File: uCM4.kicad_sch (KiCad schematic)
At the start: 71 parts, among them IC1 MAX17048G+, J10 USB_C_Receptacle, J12 Conn_02x08_Odd_Even, J13 Conn_02x07_Odd_Even, J2 Micro_SD_Card_Det, J4 Conn_01x04, J5 DummyJ, J6 DummyJ, J8 Camera 0, J9 Camera 1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

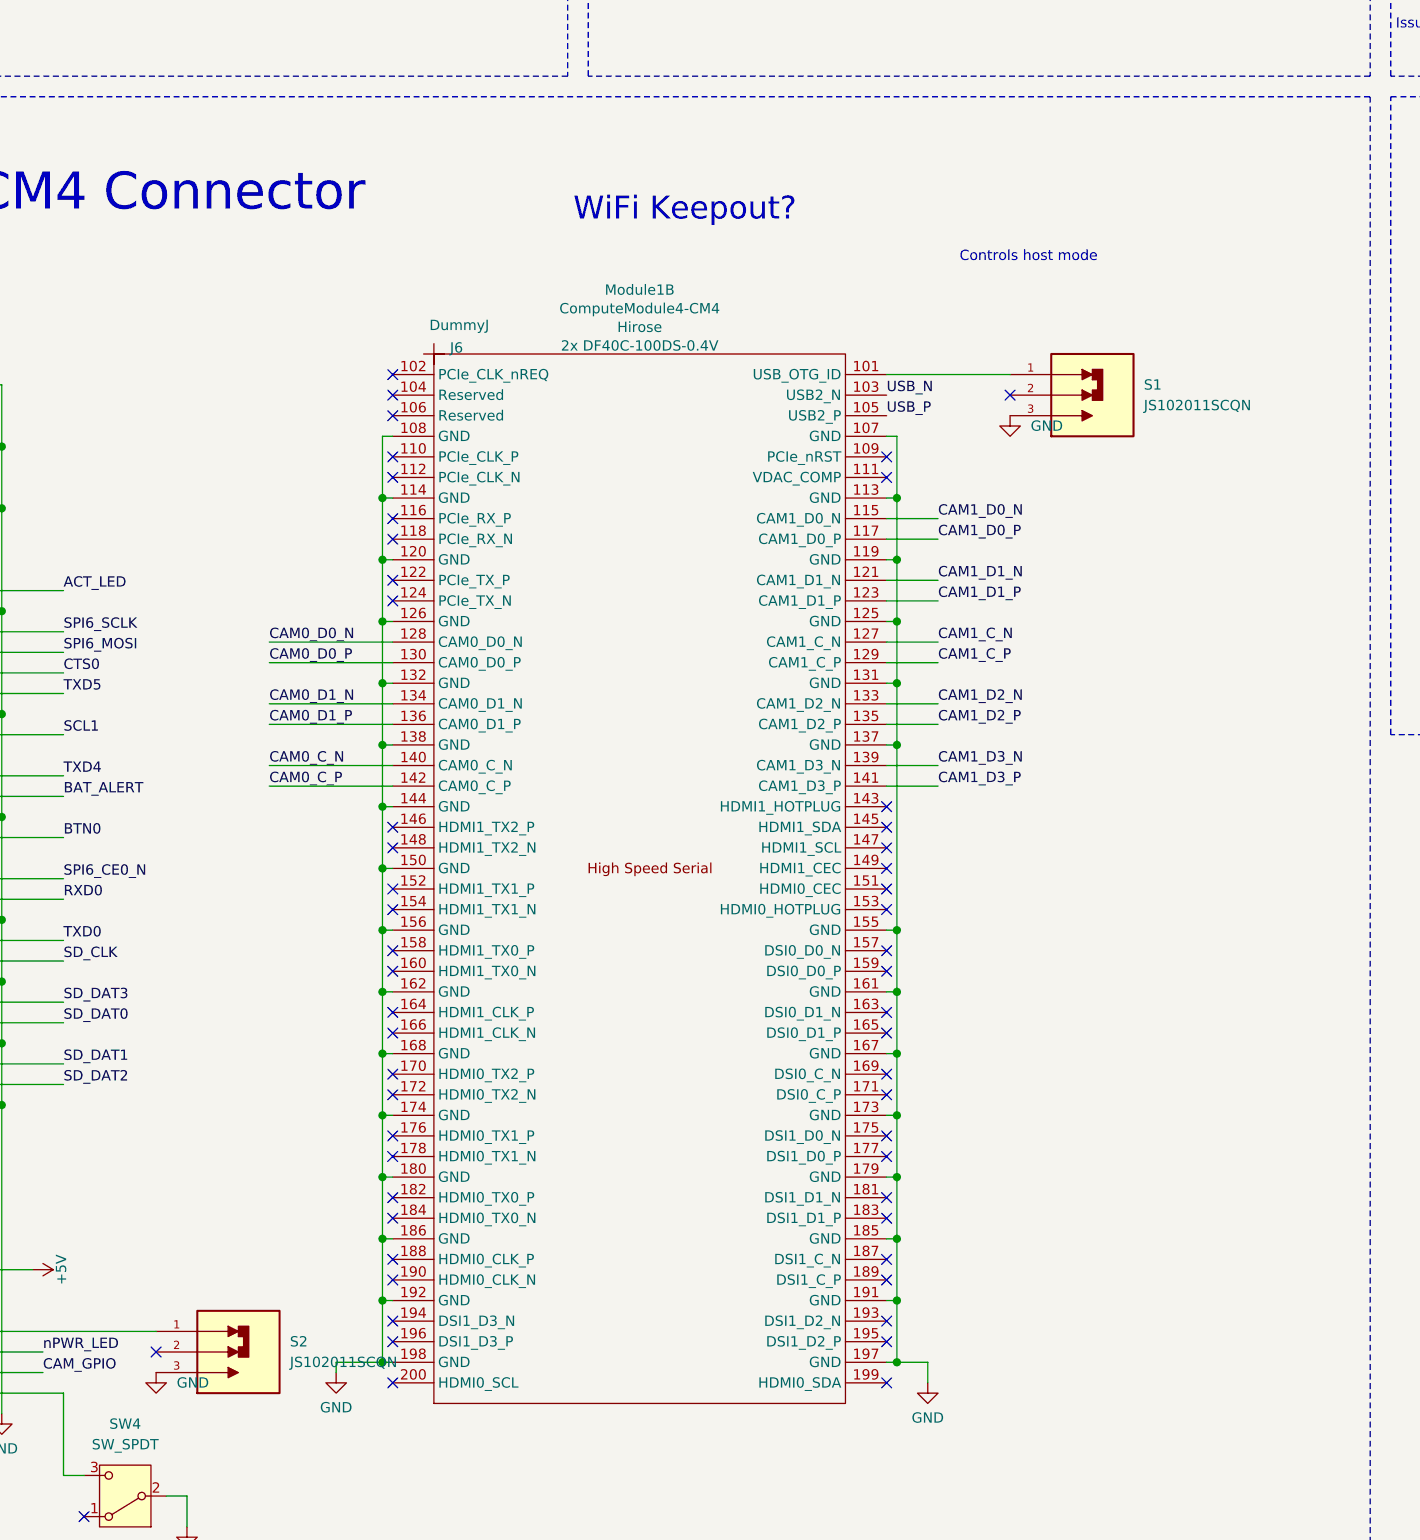
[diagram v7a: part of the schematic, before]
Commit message: Fixed switches.
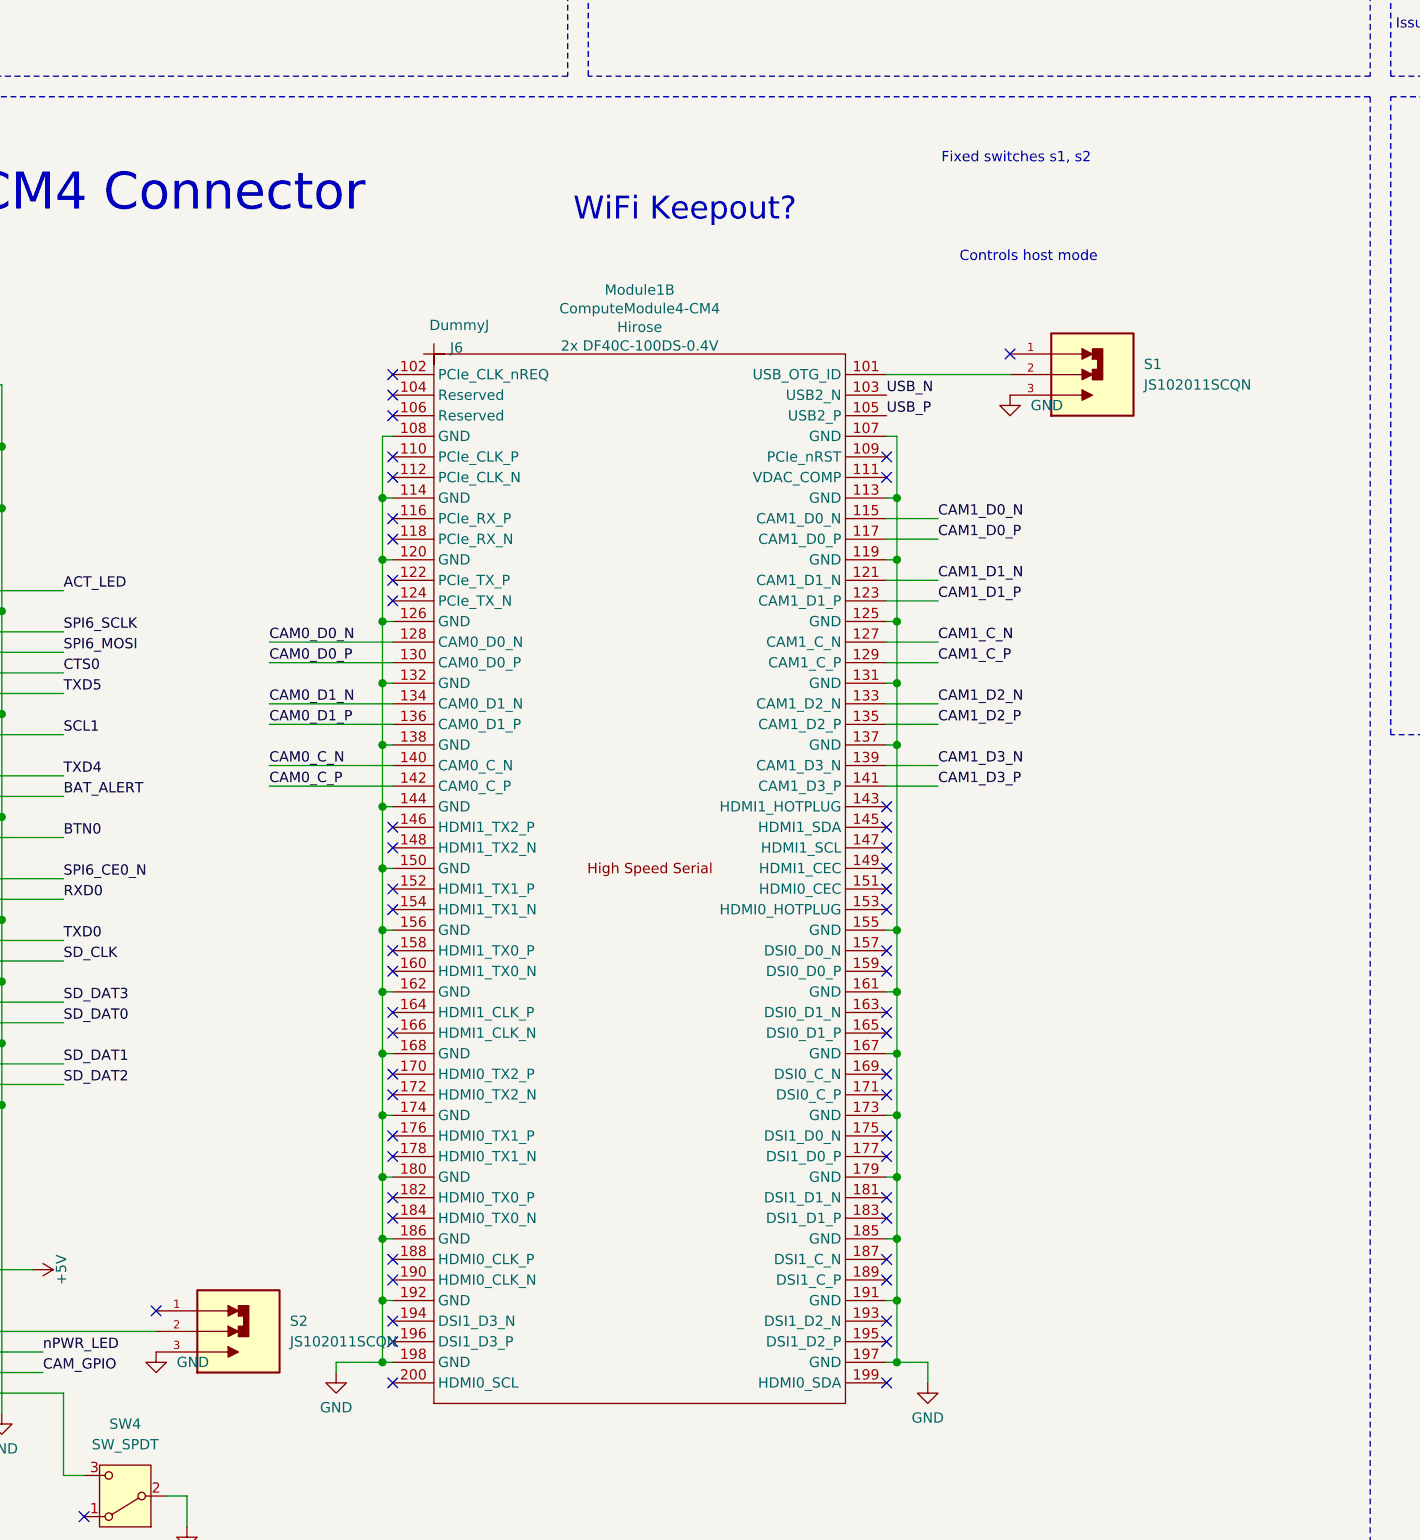
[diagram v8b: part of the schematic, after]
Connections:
- net at Module1.101 (USB_OTG_ID): now also S1.2; no longer S1.1
- net at S2.1: no longer Module1.93 (nRPIBOOT)
- net at S2.2: now also Module1.93 (nRPIBOOT)
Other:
- note added: "Fixed switches s1, s2"
- moved on the sheet: S1, S2
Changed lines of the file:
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@@
 		)
 	)
+	(text "Fixed switches s1, s2"
+		(exclude_from_sim no)
+		(at 267.462 187.96 0)
+		(effects
+			(font
+				(size 1.27 1.27)
+				(color 255 0 7 1)
+			)
+		)
+	)
 	(text "Power path"
 		(exclude_from_sim no)
@@
 	)
 	(no_connect
-		(at 80.01 228.6)
+		(at 161.29 330.2)
 	)
 	(no_connect
-		(at 170.18 81.28)
+		(at 80.01 228.6)
 	)
 	(no_connect
-		(at 161.29 335.28)
+		(at 170.18 81.28)
 	)
 	(no_connect
@@
 	)
 	(no_connect
+		(at 266.7 212.09)
+	)
+	(no_connect
 		(at 140.97 261.62)
 	)
@@
 	)
 	(no_connect
-		(at 266.7 217.17)
-	)
-	(no_connect
 		(at 140.97 236.22)
 	)
@@
 	(symbol
 		(lib_id "CM4IO:JS102011SCQN")
-		(at 171.45 335.28 0)
+		(at 171.45 332.74 0)
 		(unit 1)
 		(exclude_from_sim no)
@@
 		(fields_autoplaced yes)
 		(property "Reference" "S2"
-			(at 177.8 334.0099 0)
+			(at 177.8 331.4699 0)
 			(effects
 				(font
@@
 		)
 		(property "Value" "JS102011SCQN"
-			(at 177.8 336.5499 0)
+			(at 177.8 334.0099 0)
 			(effects
 				(font
@@
 		)
 		(property "Footprint" "CM4:SW_JS102011SCQN"
-			(at 171.45 335.28 0)
+			(at 171.45 332.74 0)
 			(effects
 				(font
@@
 		)
 		(property "Datasheet" ""
-			(at 171.45 335.28 0)
+			(at 171.45 332.74 0)
 			(effects
 				(font
@@
 		)
 		(property "Description" ""
-			(at 171.45 335.28 0)
+			(at 171.45 332.74 0)
 			(effects
 				(font
@@
 		)
 		(property "MF" "C&K"
-			(at 171.45 335.28 0)
+			(at 171.45 332.74 0)
 			(effects
 				(font
@@
 		)
 		(property "MAXIMUM_PACKAGE_HEIGHT" "5.5mm"
-			(at 171.45 335.28 0)
+			(at 171.45 332.74 0)
 			(effects
 				(font
@@
 		)
 		(property "Package" "None"
-			(at 171.45 335.28 0)
+			(at 171.45 332.74 0)
 			(effects
 				(font
@@
 		)
 		(property "Price" "None"
-			(at 171.45 335.28 0)
+			(at 171.45 332.74 0)
 			(effects
 				(font
@@
 		)
 		(property "Check_prices" "https://www.snapeda.com/parts/JS102011SCQN/C%2526K/view-part/?ref=eda"
-			(at 171.45 335.28 0)
+			(at 171.45 332.74 0)
 			(effects
 				(font
@@
 		)
 		(property "STANDARD" "Manufacturer Recommendations"
-			(at 171.45 335.28 0)
+			(at 171.45 332.74 0)
 			(effects
 				(font
@@
 		)
 		(property "PARTREV" "8 Oct 21"
-			(at 171.45 335.28 0)
+			(at 171.45 332.74 0)
 			(effects
 				(font
@@
 		)
 		(property "SnapEDA_Link" "https://www.snapeda.com/parts/JS102011SCQN/C%2526K/view-part/?ref=snap"
-			(at 171.45 335.28 0)
+			(at 171.45 332.74 0)
 			(effects
 				(font
@@
 		)
 		(property "MP" "JS102011SCQN"
-			(at 171.45 335.28 0)
+			(at 171.45 332.74 0)
 			(effects
 				(font
@@
 		)
 		(property "Description_1" "Slide Switch SPDT Surface Mount"
-			(at 171.45 335.28 0)
+			(at 171.45 332.74 0)
 			(effects
 				(font
@@
 		)
 		(property "Availability" "In Stock"
-			(at 171.45 335.28 0)
+			(at 171.45 332.74 0)
 			(effects
 				(font
@@
 		)
 		(property "MANUFACTURER" "C&K"
-			(at 171.45 335.28 0)
+			(at 171.45 332.74 0)
 			(effects
 				(font
@@
 		)
 		(property "LCSC Part #" "C221661"
-			(at 171.45 335.28 0)
+			(at 171.45 332.74 0)
 			(effects
 				(font
@@
 		(lib_name "GND_8")
 		(lib_id "power:GND")
-		(at 266.7 219.71 0)
+		(at 266.7 217.17 0)
 		(unit 1)
 		(exclude_from_sim no)
@@
 		(fields_autoplaced yes)
 		(property "Reference" "#PWR014"
-			(at 266.7 226.06 0)
+			(at 266.7 223.52 0)
 			(effects
 				(font
@@
 		)
 		(property "Value" "GND"
-			(at 269.24 220.9799 0)
+			(at 269.24 218.4399 0)
 			(effects
 				(font
@@
 		)
 		(property "Footprint" ""
-			(at 266.7 219.71 0)
+			(at 266.7 217.17 0)
 			(effects
 				(font
@@
 		)
 		(property "Datasheet" ""
-			(at 266.7 219.71 0)
+			(at 266.7 217.17 0)
 			(effects
 				(font
@@
 		)
 		(property "Description" "Power symbol creates a global label with name \"GND\" , ground"
-			(at 266.7 219.71 0)
+			(at 266.7 217.17 0)
 			(effects
 				(font
@@
 	(symbol
 		(lib_id "CM4IO:JS102011SCQN")
-		(at 276.86 217.17 0)
+		(at 276.86 214.63 0)
 		(unit 1)
 		(exclude_from_sim no)
@@
 		(fields_autoplaced yes)
 		(property "Reference" "S1"
-			(at 283.21 215.8999 0)
+			(at 283.21 213.3599 0)
 			(effects
 				(font
@@
 		)
 		(property "Value" "JS102011SCQN"
-			(at 283.21 218.4399 0)
+			(at 283.21 215.8999 0)
 			(effects
 				(font
@@
 		)
 		(property "Footprint" "CM4:SW_JS102011SCQN"
-			(at 276.86 217.17 0)
+			(at 276.86 214.63 0)
 			(effects
 				(font
@@
 		)
 		(property "Datasheet" ""
-			(at 276.86 217.17 0)
+			(at 276.86 214.63 0)
 			(effects
 				(font
@@
 		)
 		(property "Description" ""
-			(at 276.86 217.17 0)
+			(at 276.86 214.63 0)
 			(effects
 				(font
@@
 		)
 		(property "MF" "C&K"
-			(at 276.86 217.17 0)
+			(at 276.86 214.63 0)
 			(effects
 				(font
@@
 		)
 		(property "MAXIMUM_PACKAGE_HEIGHT" "5.5mm"
-			(at 276.86 217.17 0)
+			(at 276.86 214.63 0)
 			(effects
 				(font
@@
 		)
 		(property "Package" "None"
-			(at 276.86 217.17 0)
+			(at 276.86 214.63 0)
 			(effects
 				(font
@@
 		)
 		(property "Price" "None"
-			(at 276.86 217.17 0)
+			(at 276.86 214.63 0)
 			(effects
 				(font
@@
 		)
 		(property "Check_prices" "https://www.snapeda.com/parts/JS102011SCQN/C%2526K/view-part/?ref=eda"
-			(at 276.86 217.17 0)
+			(at 276.86 214.63 0)
 			(effects
 				(font
@@
 		)
 		(property "STANDARD" "Manufacturer Recommendations"
-			(at 276.86 217.17 0)
+			(at 276.86 214.63 0)
 			(effects
 				(font
@@
 		)
 		(property "PARTREV" "8 Oct 21"
-			(at 276.86 217.17 0)
+			(at 276.86 214.63 0)
 			(effects
 				(font
@@
 		)
 		(property "SnapEDA_Link" "https://www.snapeda.com/parts/JS102011SCQN/C%2526K/view-part/?ref=snap"
-			(at 276.86 217.17 0)
+			(at 276.86 214.63 0)
 			(effects
 				(font
@@
 		)
 		(property "MP" "JS102011SCQN"
-			(at 276.86 217.17 0)
+			(at 276.86 214.63 0)
 			(effects
 				(font
@@
 		)
 		(property "Description_1" "Slide Switch SPDT Surface Mount"
-			(at 276.86 217.17 0)
+			(at 276.86 214.63 0)
 			(effects
 				(font
@@
 		)
 		(property "Availability" "In Stock"
-			(at 276.86 217.17 0)
+			(at 276.86 214.63 0)
 			(effects
 				(font
@@
 		)
 		(property "MANUFACTURER" "C&K"
-			(at 276.86 217.17 0)
+			(at 276.86 214.63 0)
 			(effects
 				(font
@@
 		)
 		(property "LCSC Part #" "C221661"
-			(at 276.86 217.17 0)
+			(at 276.86 214.63 0)
 			(effects
 				(font
@@
 		)
 		(instances
-			(project ""
+			(project "uCM4"
 				(path "/ab308ddb-f5b4-4376-8062-4d719b3e690f"
 					(reference "S1")
@@
 		(lib_name "GND_8")
 		(lib_id "power:GND")
-		(at 161.29 337.82 0)
+		(at 161.29 335.28 0)
 		(unit 1)
 		(exclude_from_sim no)
@@
 		(fields_autoplaced yes)
 		(property "Reference" "#PWR09"
-			(at 161.29 344.17 0)
+			(at 161.29 341.63 0)
 			(effects
 				(font
@@
 		)
 		(property "Value" "GND"
-			(at 163.83 339.0899 0)
+			(at 163.83 336.5499 0)
 			(effects
 				(font
@@
 		)
 		(property "Footprint" ""
-			(at 161.29 337.82 0)
+			(at 161.29 335.28 0)
 			(effects
 				(font
@@
 		)
 		(property "Datasheet" ""
-			(at 161.29 337.82 0)
+			(at 161.29 335.28 0)
 			(effects
 				(font
@@
 		)
 		(property "Description" "Power symbol creates a global label with name \"GND\" , ground"
-			(at 161.29 337.82 0)
+			(at 161.29 335.28 0)
 			(effects
 				(font
